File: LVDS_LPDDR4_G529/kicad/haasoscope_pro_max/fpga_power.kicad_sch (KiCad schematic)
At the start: 1 part, among them U3 Ti90G529_Functions

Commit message: Aligned schematics, sort of
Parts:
- removed unit 7 of U3
- added unit 9 of U3
- U3: footprint G529:BGA-529_23x23_19.0x19.0mm -> haasoscope_pro_adc_fpga_board:BGA-529_23x23_19.0x19.0mm

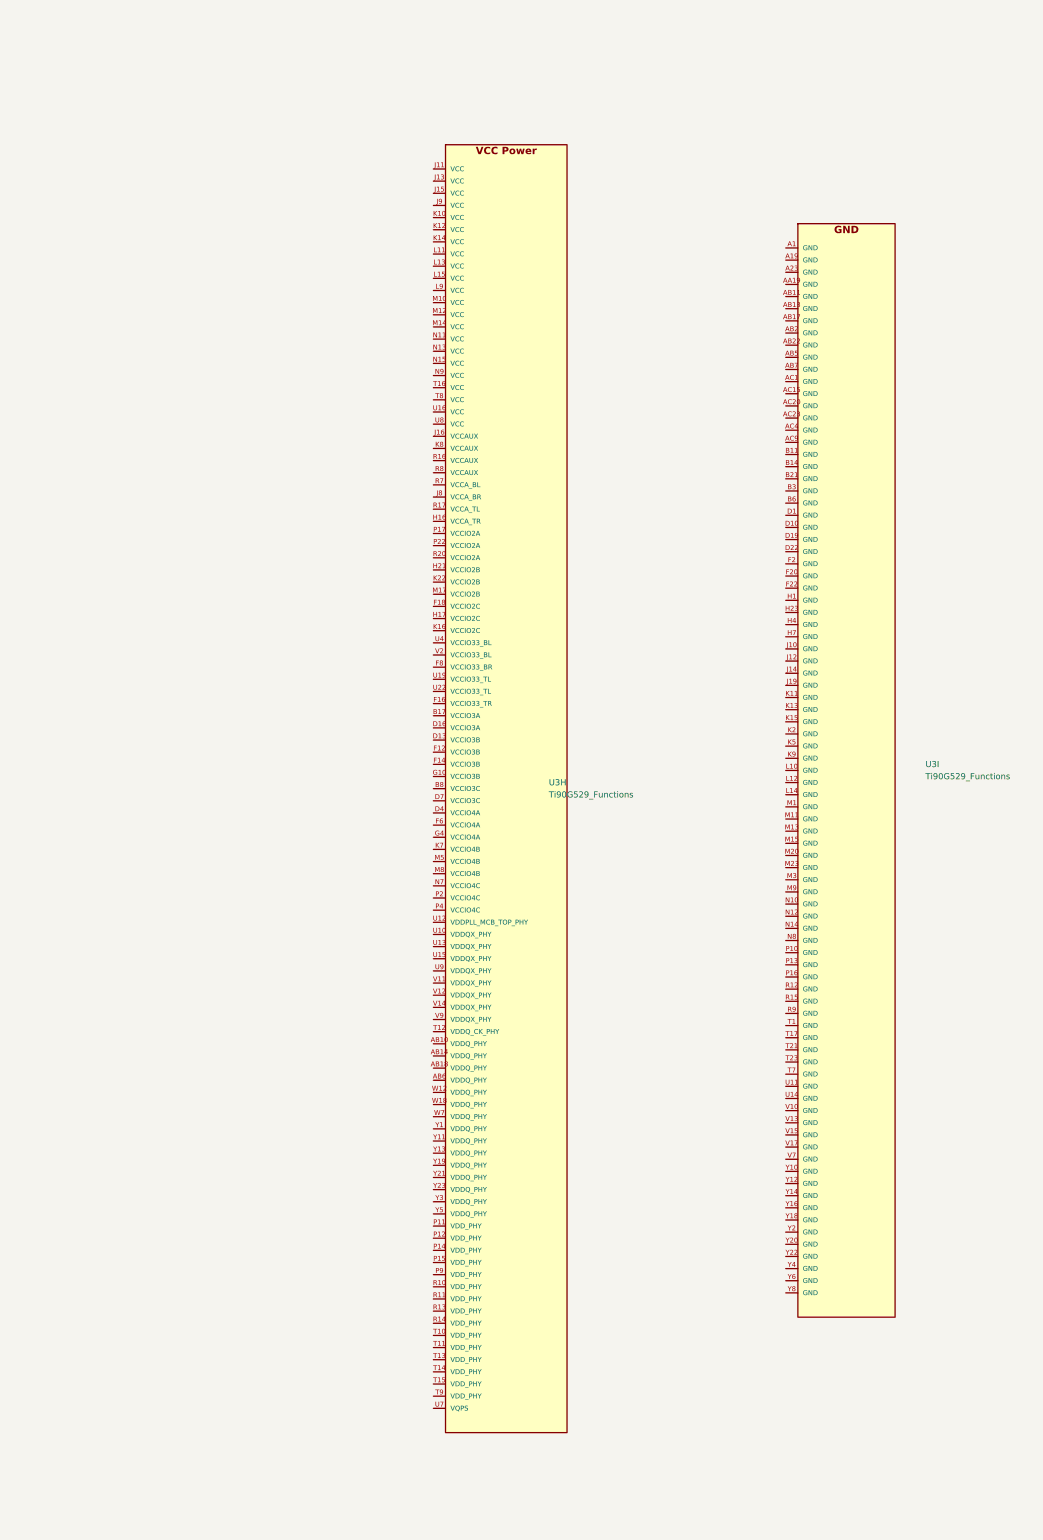
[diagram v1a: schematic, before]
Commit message: Aligned schematics, better
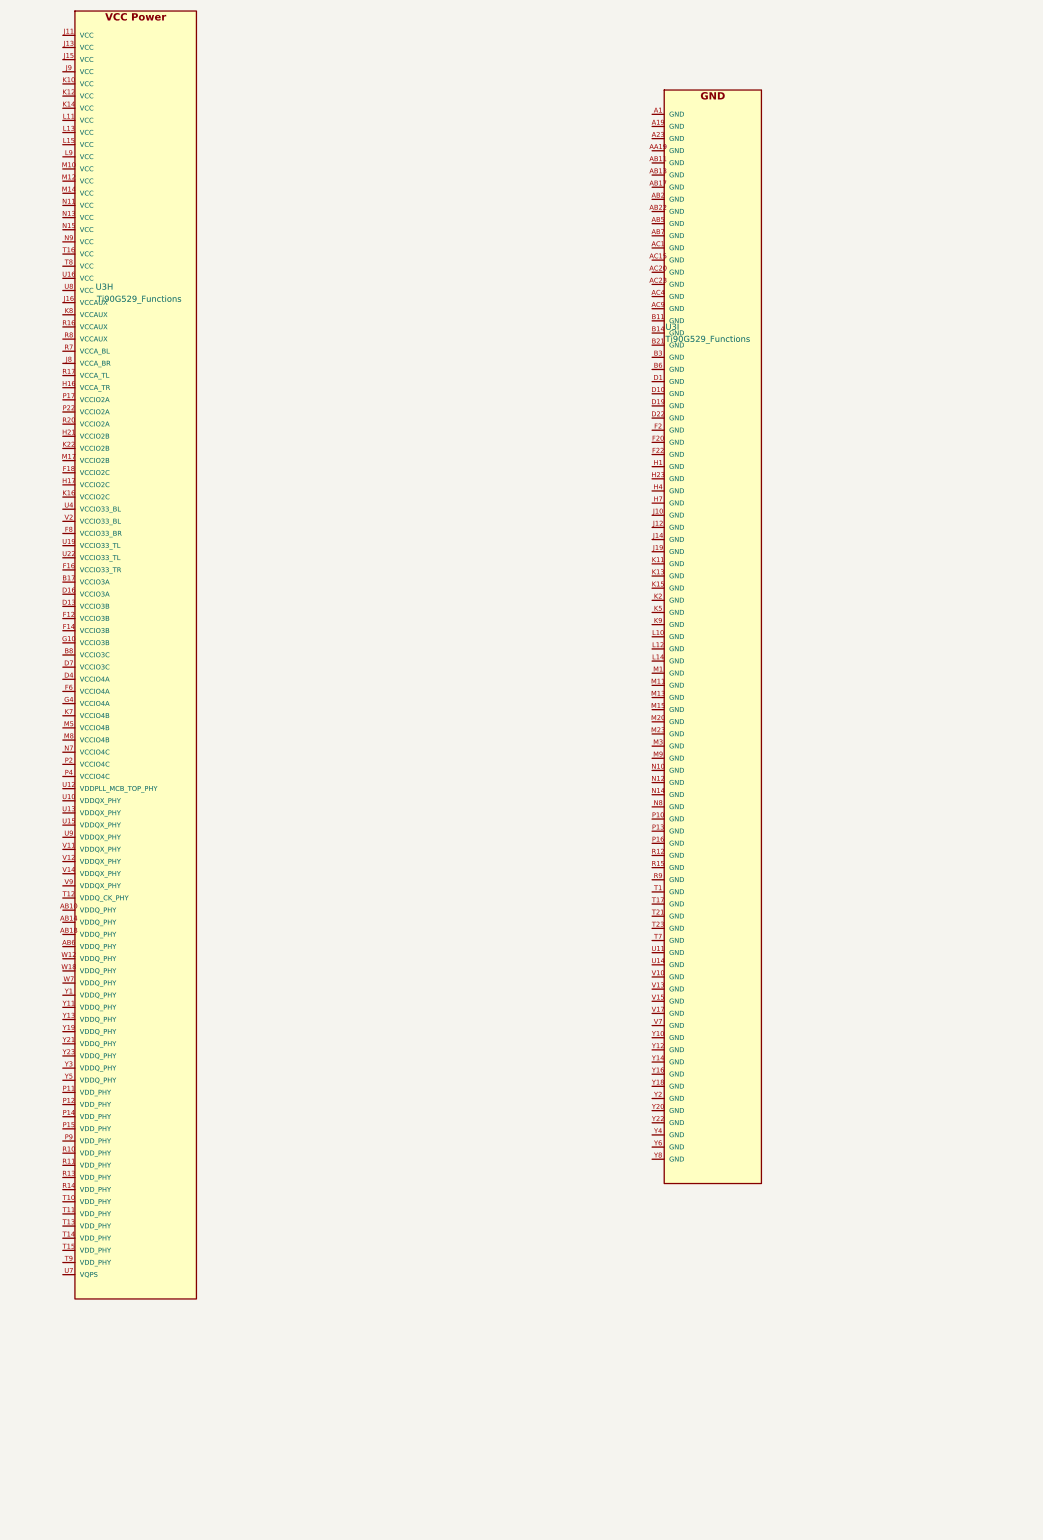
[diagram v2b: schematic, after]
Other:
- moved on the sheet: U3H, U3I
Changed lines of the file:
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@@
 	(symbol
 		(lib_id "Ti90G529_Functions:Ti90G529_Functions")
-		(at 154.94 134.62 0)
+		(at 77.47 106.68 0)
 		(unit 8)
 		(exclude_from_sim no)
@@
 		(on_board yes)
 		(dnp no)
-		(fields_autoplaced yes)
 		(property "Reference" "U3"
-			(at 176.53 133.3352 0)
+			(at 81.788 29.718 0)
 			(effects
 				(font
@@
 		)
 		(property "Value" "Ti90G529_Functions"
-			(at 176.53 135.8752 0)
+			(at 82.042 32.258 0)
 			(effects
 				(font
@@
 		)
 		(property "Footprint" "haasoscope_pro_adc_fpga_board:BGA-529_23x23_19.0x19.0mm"
-			(at 154.94 138.43 0)
+			(at 77.47 110.49 0)
 			(effects
 				(font
@@
 		)
 		(property "Datasheet" ""
-			(at 154.94 140.97 0)
+			(at 77.47 113.03 0)
 			(effects
 				(font
@@
 		)
 		(property "Description" "Efinix Ti90G529 FPGA organized by peripheral interface"
-			(at 154.94 143.51 0)
+			(at 77.47 115.57 0)
 			(effects
 				(font
@@
 	(symbol
 		(lib_id "Ti90G529_Functions:Ti90G529_Functions")
-		(at 228.6 130.81 0)
+		(at 200.66 102.87 0)
 		(unit 9)
 		(exclude_from_sim no)
@@
 		(on_board yes)
 		(dnp no)
-		(fields_autoplaced yes)
 		(property "Reference" "U3"
-			(at 255.27 129.5252 0)
+			(at 200.914 38.1 0)
 			(effects
 				(font
@@
 		)
 		(property "Value" "Ti90G529_Functions"
-			(at 255.27 132.0652 0)
+			(at 200.914 40.64 0)
 			(effects
 				(font
@@
 		)
 		(property "Footprint" "haasoscope_pro_adc_fpga_board:BGA-529_23x23_19.0x19.0mm"
-			(at 228.6 134.62 0)
+			(at 200.66 106.68 0)
 			(effects
 				(font
@@
 		)
 		(property "Datasheet" ""
-			(at 228.6 137.16 0)
+			(at 200.66 109.22 0)
 			(effects
 				(font
@@
 		)
 		(property "Description" "Efinix Ti90G529 FPGA organized by peripheral interface"
-			(at 228.6 139.7 0)
+			(at 200.66 111.76 0)
 			(effects
 				(font

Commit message: Aligned schematics, connected some components
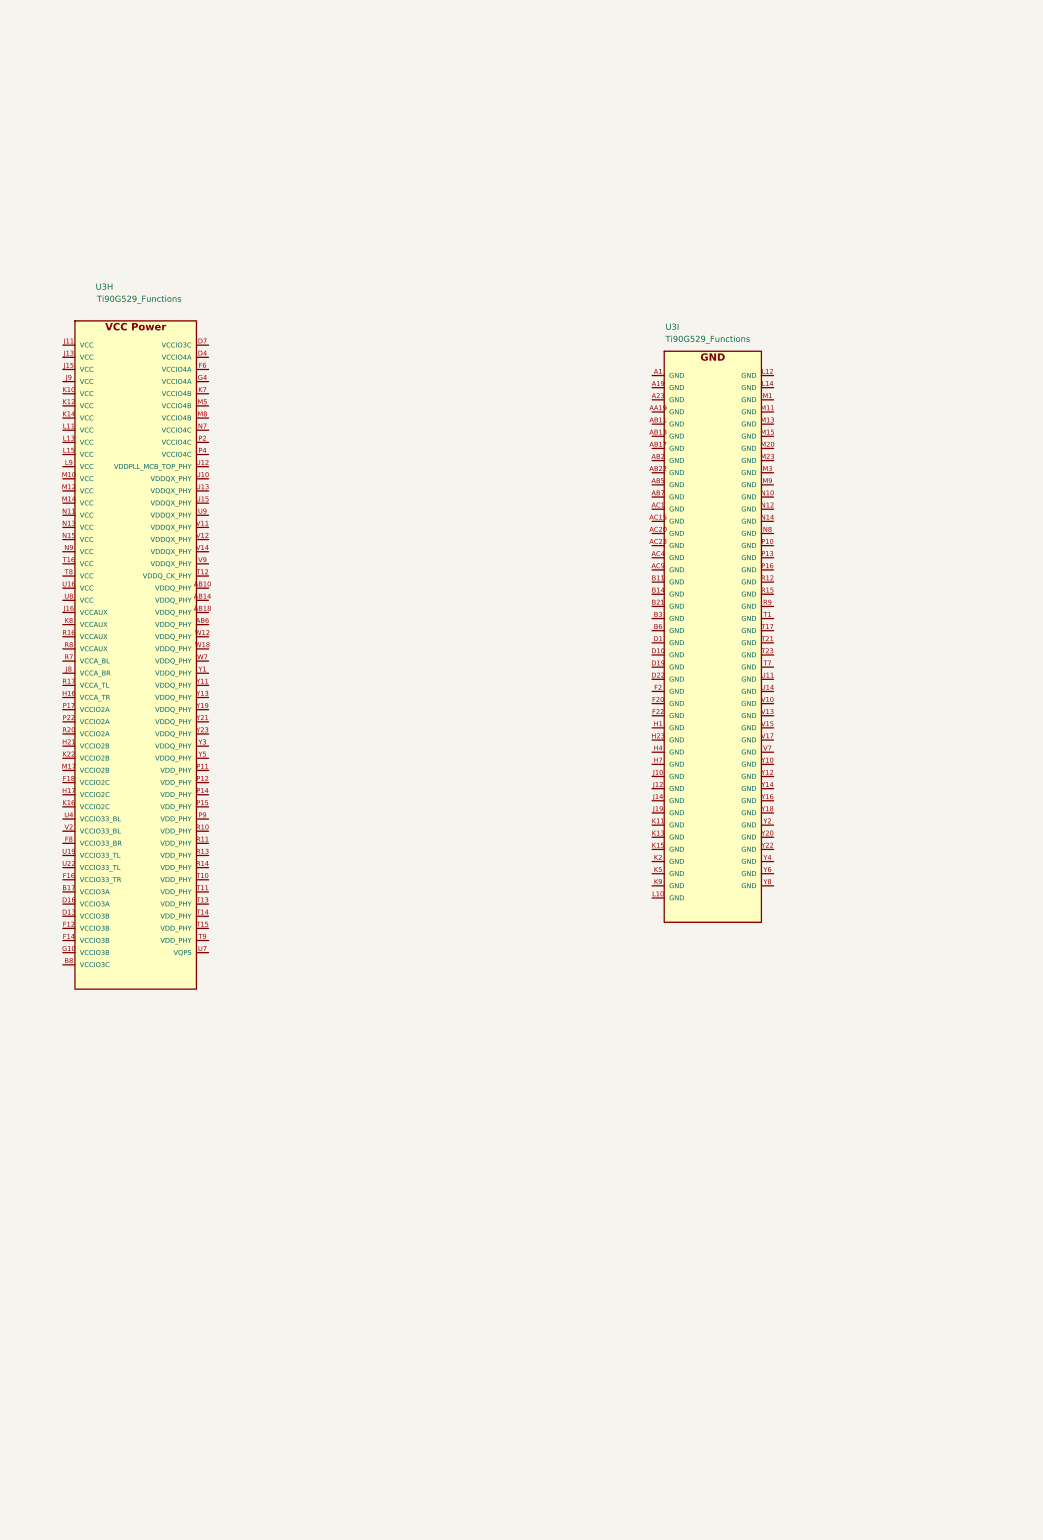
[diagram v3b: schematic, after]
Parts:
- U3: footprint haasoscope_pro_adc_fpga_board:BGA-529_23x23_19.0x19.0mm -> G529:BGA-529_23x23_19.0x19.0mm
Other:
- moved on the sheet: U3H, U3I
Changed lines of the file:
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@@
 			)
 		)
-		(property "Footprint" "haasoscope_pro_adc_fpga_board:BGA-529_23x23_19.0x19.0mm"
+		(property "Footprint" "G529:BGA-529_23x23_19.0x19.0mm"
 			(at 77.47 110.49 0)
 			(effects
@@
 			)
 		)
-		(property "Footprint" "haasoscope_pro_adc_fpga_board:BGA-529_23x23_19.0x19.0mm"
+		(property "Footprint" "G529:BGA-529_23x23_19.0x19.0mm"
 			(at 200.66 106.68 0)
 			(effects
